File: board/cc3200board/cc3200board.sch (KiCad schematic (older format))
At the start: 26 parts

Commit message: Added datasheet for SPI flash part
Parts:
- removed C?: 10uF, ~, symbol CPSMALL
- removed U?: CC3200R1M2RGCR, VQFN64, symbol CC3200R1M2RGCR
- added C12: 10uF, ~, symbol CPSMALL
- added C46: 10pF, ~, symbol CPSMALL
- added R2, R3, R4: 100K, ~, symbol R
- added U?: CC3200R1M2RGCR, VQFN64, symbol CC3200R1M2RGCR
- added U?: N25Q128A13ESE40E, ~, symbol N25Q128A13ESE40E
- C24: renamed from C?; value 10uF -> 10pF
- X1: renamed from X?; value CRYSTAL -> 32.768kH
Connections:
- wire segments 95 -> 112
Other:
- moved on the sheet: L2, L3, L8, R1, X1

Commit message: Finalized power/RF subsystems for CC3200board
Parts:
- added C42: 6.2pF, ~, symbol CPsmall
- added C49: 10pF, ~, symbol CPsmall
- added C9: 1.0pF, ~, symbol CPsmall
- added E1: ANT, symbol ANT
- added F1: FLT24, symbol FLT24
- added L1: 3.6nH, ~, symbol INDUCTOR_SMALL
- added X2: 40M, symbol 4-PIN_XTAL
- C1, C10, C11, C12, C13, C14, C15, C16, C17, C18, C19, C2, C20, C22, C23, C24, C3, C4, C46, C5, C8: symbol CPSMALL -> CPsmall
- gave numbers to parts that had none: 1
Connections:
- wire segments 112 -> 174

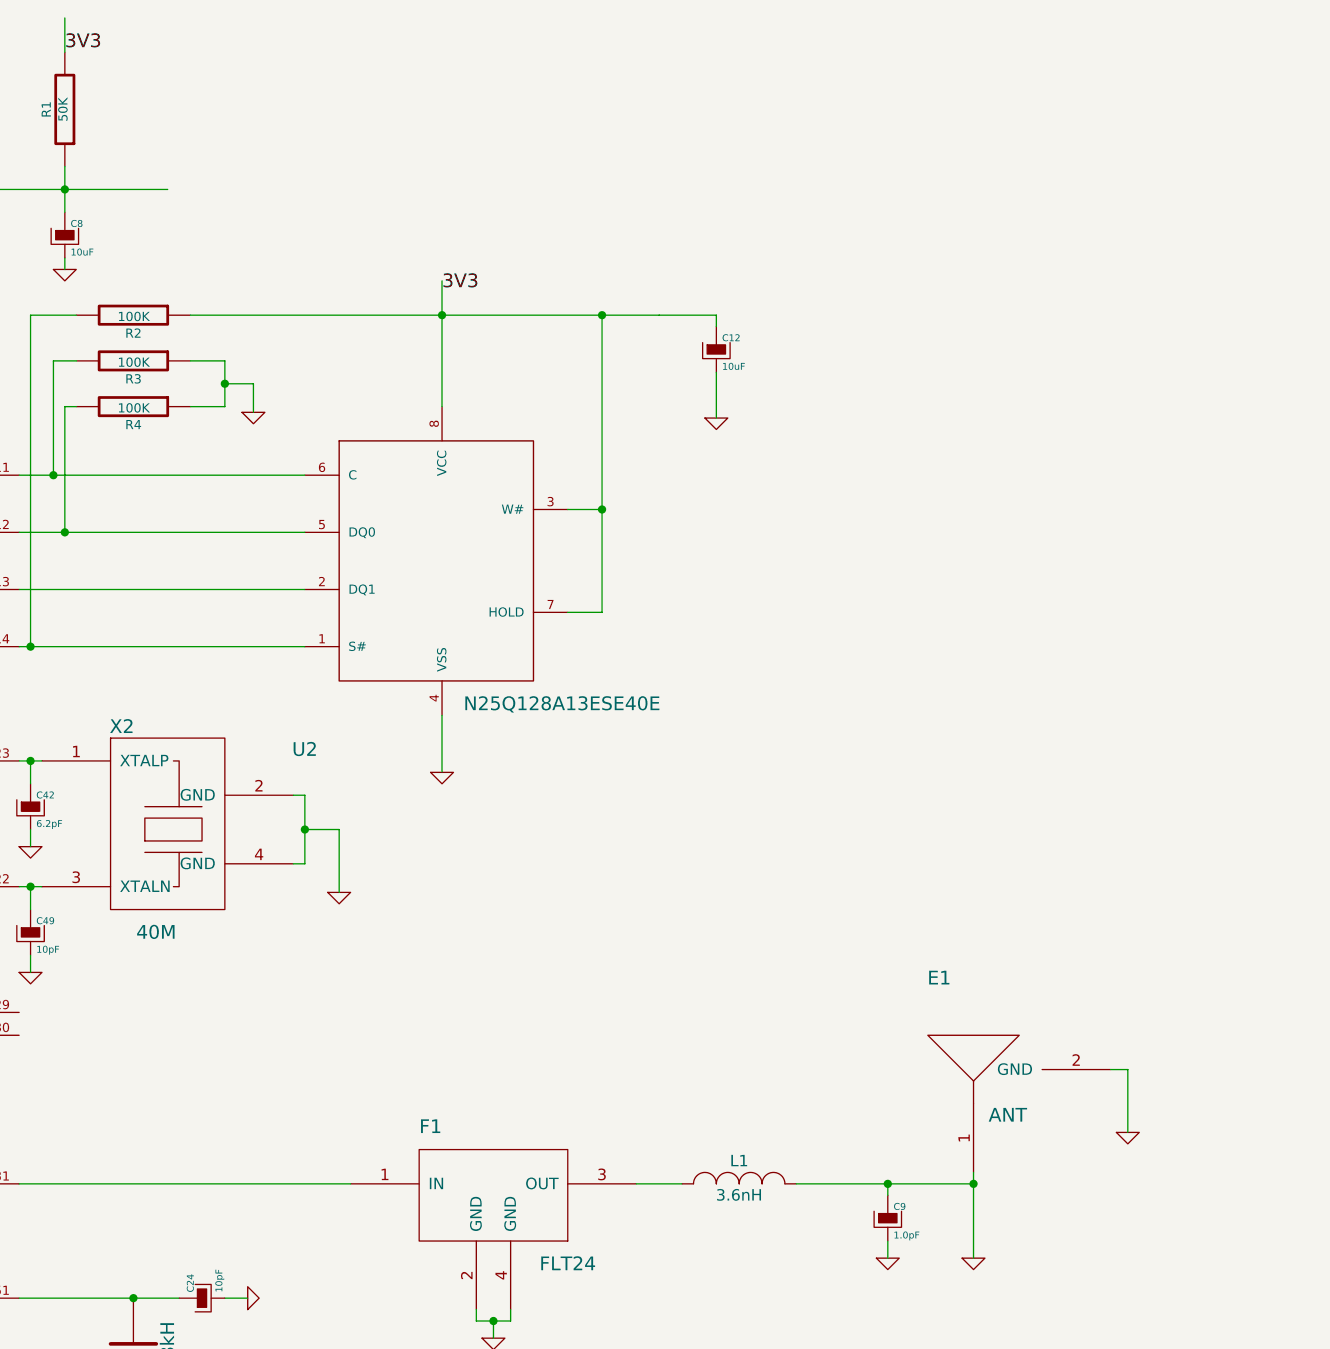
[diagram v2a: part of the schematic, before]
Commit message: Added initial GPIO/JTAG/SOP breakout pins. Impedance controlled traces labelled.
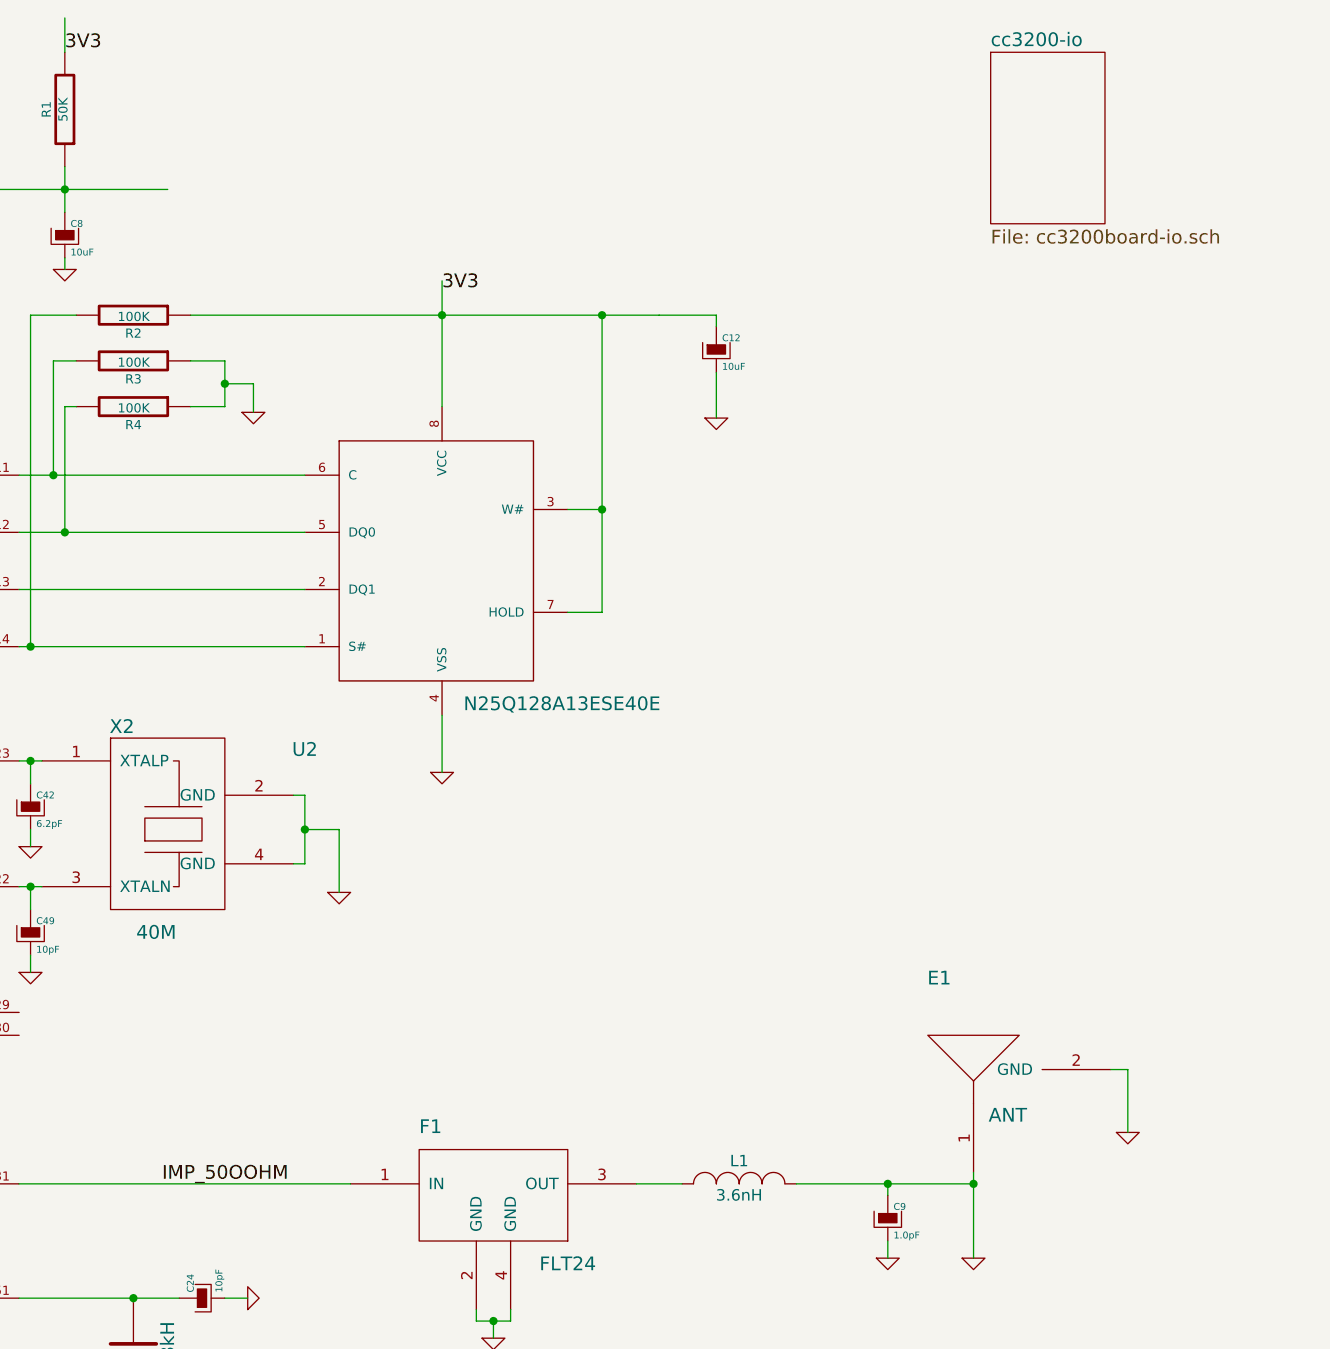
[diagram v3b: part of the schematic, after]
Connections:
- net labels added: IMP_50OOHM
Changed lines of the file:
@@
 $Descr A4 11693 8268
 encoding utf-8
-Sheet 1 1
+Sheet 1 2
 Title ""
 Date "31 oct 2014"
@@
 	8100 2700 8250 2700
 Connection ~ 8250 2700
+$Sheet
+S 9950 700  500  750
+U 5452FF59
+F0 "cc3200-io" 60
+F1 "cc3200board-io.sch" 60
+$EndSheet
+Text Label 6325 5650 0    60   ~ 0
+IMP_50OOHM
 $EndSCHEMATC

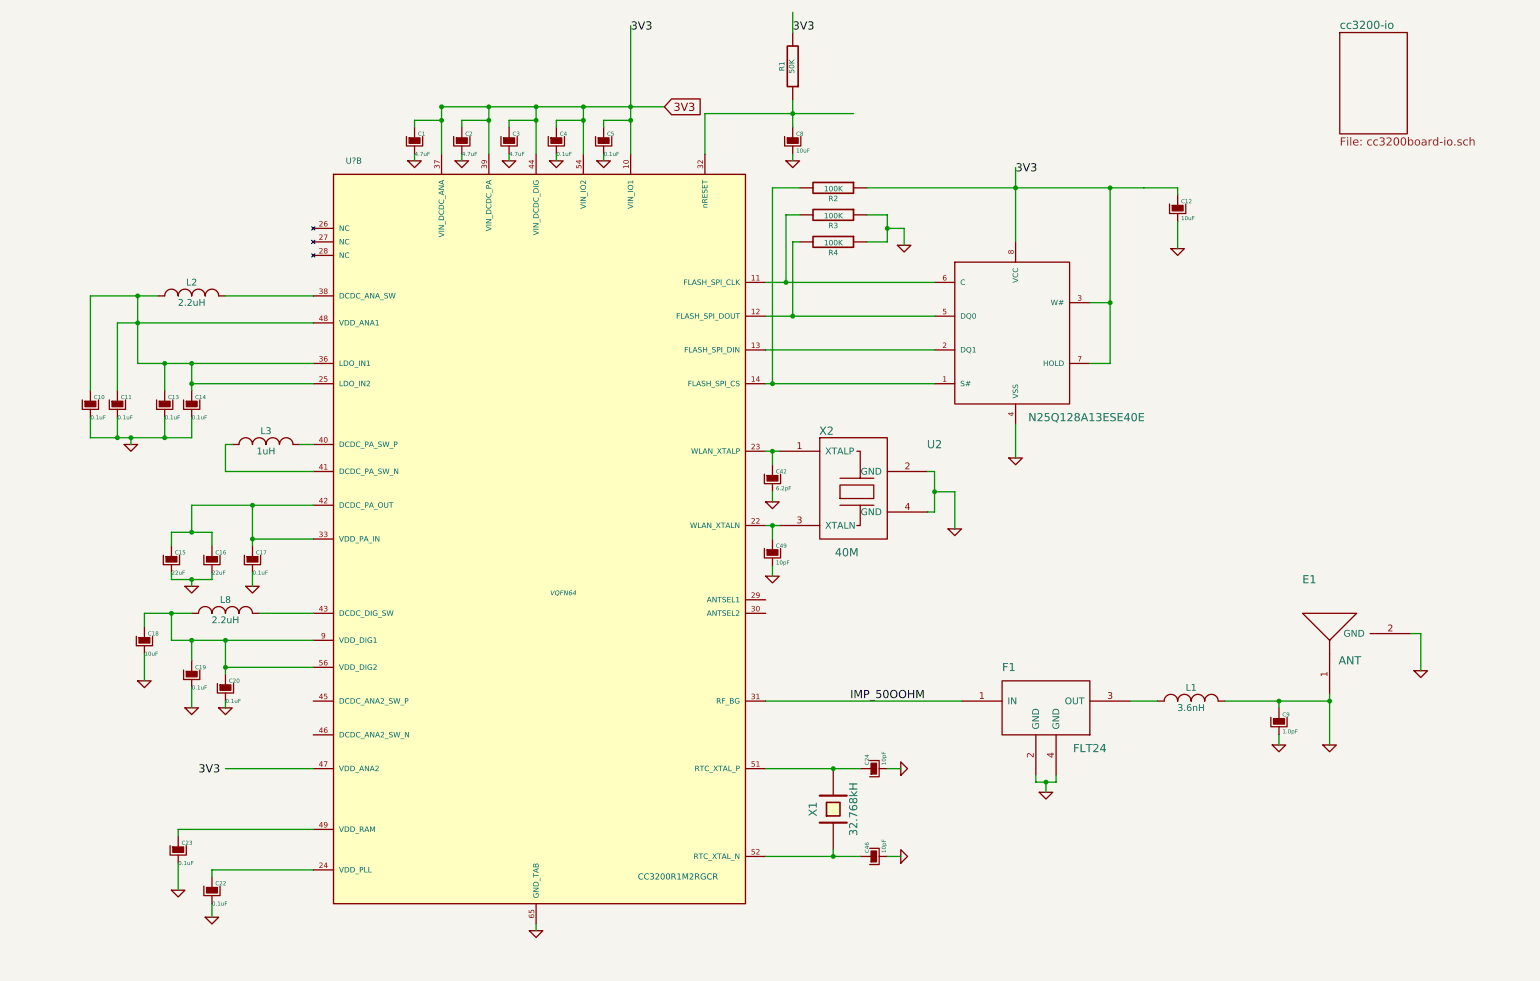
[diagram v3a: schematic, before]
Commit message: Added footprints for all CC3200 components
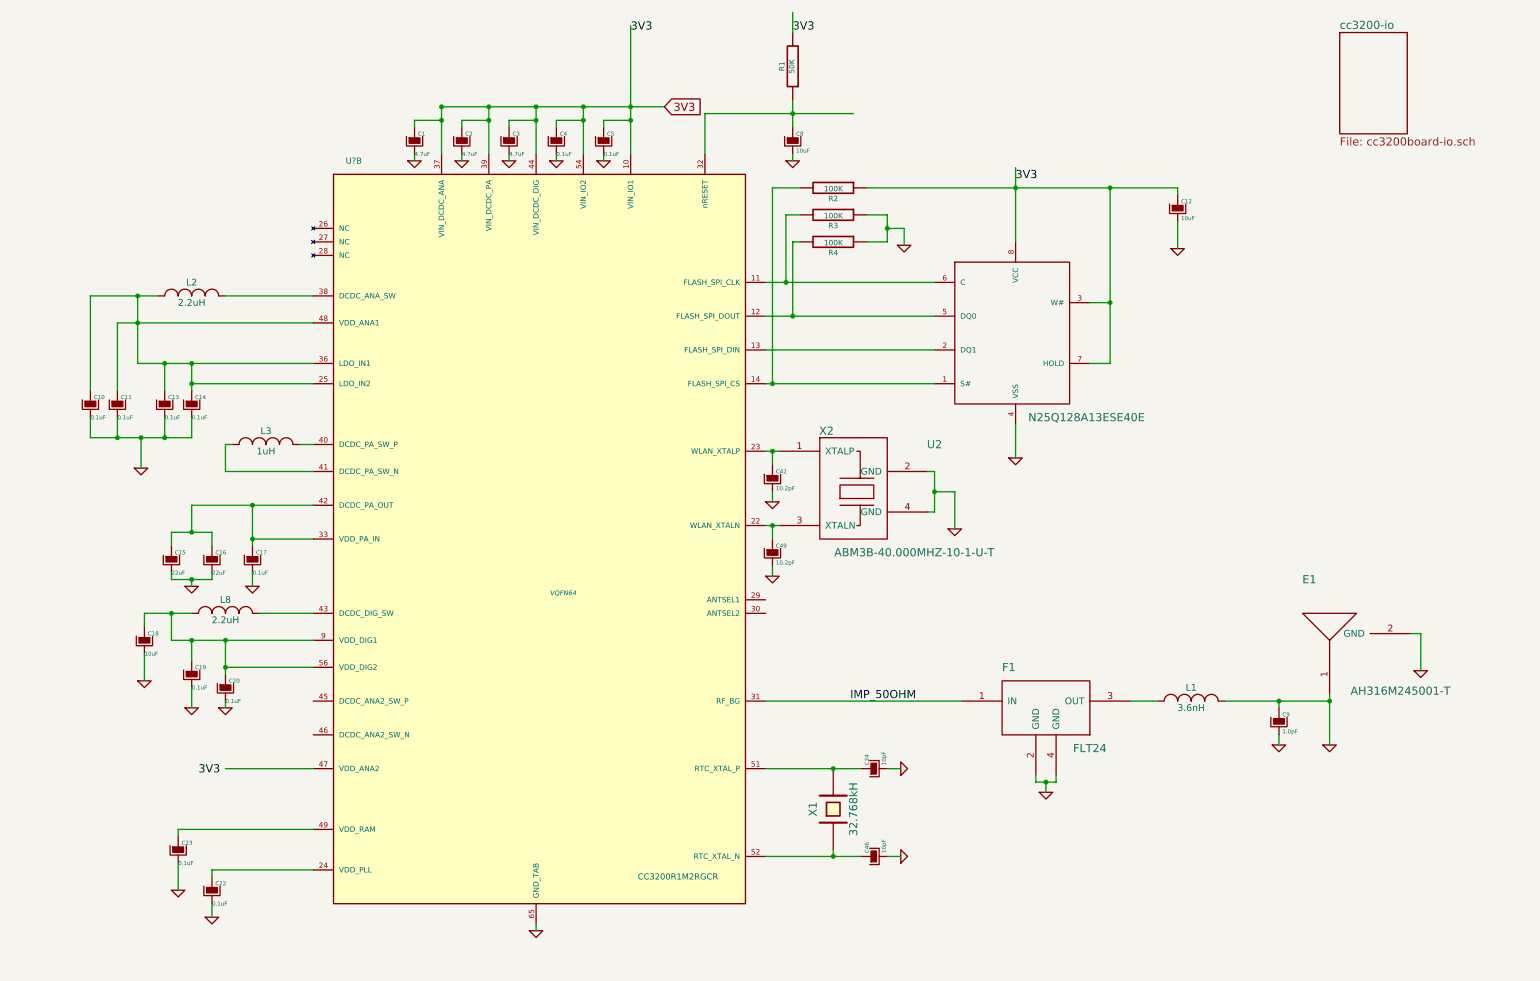
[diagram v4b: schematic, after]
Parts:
- C42: value 6.2pF -> 10.2pF
- C49: value 10pF -> 10.2pF
- E1: value ANT -> AH316M245001-T
- X2: value 40M -> ABM3B-40.000MHZ-10-1-U-T
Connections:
- net labels added: IMP_50OHM
- net labels removed: IMP_50OOHM
- wire segments 174 -> 128
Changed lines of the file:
@@
 L GND #PWR?
 U 1 1 5446219E
-P 1000 3750
-F 0 "#PWR?" H 1000 3750 30  0001 C CNN
-F 1 "GND" H 1000 3680 30  0001 C CNN
-F 2 "" H 1000 3750 60  0000 C CNN
-F 3 "" H 1000 3750 60  0000 C CNN
-	1    1000 3750
+P 1075 3925
+F 0 "#PWR?" H 1075 3925 30  0001 C CNN
+F 1 "GND" H 1075 3855 30  0001 C CNN
+F 2 "" H 1075 3925 60  0000 C CNN
+F 3 "" H 1075 3925 60  0000 C CNN
+	1    1075 3925
 	1    0    0    -1
 $EndComp
@@
 	1    0    0    -1
 $EndComp
-Text Label 7550 1750 0    60   ~ 0
+Text Label 7550 1800 0    60   ~ 0
 3V3
 $Comp
@@
 P 6450 4100
 F 0 "X2" H 6150 4550 60  0000 C CNN
-F 1 "40M" H 6300 3650 60  0000 C CNN
+F 1 "ABM3B-40.000MHZ-10-1-U-T" H 6800 3650 60  0000 C CNN
 F 2 "" H 7250 3550 60  0000 C CNN
 F 3 "" H 7250 3550 60  0000 C CNN
@@
 P 5750 4550
 F 0 "C49" H 5775 4600 30  0000 L CNN
-F 1 "10pF" H 5775 4475 30  0000 L CNN
+F 1 "10.2pF" H 5775 4475 30  0000 L CNN
 F 2 "~" H 5750 4550 60  0000 C CNN
 F 3 "~" H 5750 4550 60  0000 C CNN
@@
 P 5750 4000
 F 0 "C42" H 5775 4050 30  0000 L CNN
-F 1 "6.2pF" H 5775 3925 30  0000 L CNN
+F 1 "10.2pF" H 5775 3925 30  0000 L CNN
 F 2 "~" H 5750 4000 60  0000 C CNN
 F 3 "~" H 5750 4000 60  0000 C CNN
@@
 P 9875 5300
 F 0 "E1" H 9725 5850 60  0000 C CNN
-F 1 "ANT" H 10025 5250 60  0000 C CNN
+F 1 "AH316M245001-T" H 10400 5025 60  0000 C CNN
 F 2 "" H 9875 5300 60  0000 C CNN
 F 3 "" H 9875 5300 60  0000 C CNN
@@
 	700  3350 700  2650
 Wire Wire Line
-	700  2650 1050 2650
-Wire Wire Line
-	1050 2650 1200 2650
+	700  2650 1200 2650
 Connection ~ 1050 2650
 Wire Wire Line
-	1050 3150 1250 3150
-Wire Wire Line
-	1250 3150 1450 3150
-Wire Wire Line
-	1450 3150 2350 3150
+	1050 3150 2350 3150
 Wire Wire Line
 	1450 3300 2350 3300
@@
 Connection ~ 1250 3150
 Wire Wire Line
-	1450 3150 1450 3300
-Wire Wire Line
-	1450 3300 1450 3350
+	1450 3150 1450 3350
 Connection ~ 1450 3300
 Wire Wire Line
@@
 	1600 7250 1600 7150
 Wire Wire Line
-	5900 1200 5900 1300
-Wire Wire Line
-	5900 1300 5900 1400
-Wire Wire Line
-	5250 1300 5900 1300
-Wire Wire Line
-	5900 1300 6350 1300
+	5900 1200 5900 1400
+Wire Wire Line
+	5250 1300 6350 1300
 Connection ~ 5900 1300
 Wire Wire Line
 	5900 1600 5900 1650
 Wire Wire Line
-	5700 6800 6200 6800
-Wire Wire Line
-	6200 6800 6400 6800
+	5700 6800 6400 6800
 Connection ~ 6200 6800
 Wire Wire Line
@@
 	4500 1650 4500 1600
 Wire Wire Line
-	3300 1250 3650 1250
-Wire Wire Line
-	3650 1250 4000 1250
-Wire Wire Line
-	4000 1250 4350 1250
-Wire Wire Line
-	4350 1250 4700 1250
-Wire Wire Line
-	4700 1250 4950 1250
+	3300 1250 4950 1250
 Wire Wire Line
 	4150 1400 4150 1350
@@
 	4150 1350 4350 1350
 Wire Wire Line
-	4350 1250 4350 1350
-Wire Wire Line
-	4350 1350 4350 1600
+	4350 1250 4350 1600
 Connection ~ 4350 1250
 Connection ~ 4350 1350
 Wire Wire Line
-	4000 1250 4000 1350
-Wire Wire Line
-	4000 1350 4000 1600
+	4000 1250 4000 1600
 Connection ~ 4000 1250
 Wire Wire Line
@@
 Connection ~ 4000 1350
 Wire Wire Line
-	3650 1250 3650 1350
-Wire Wire Line
-	3650 1350 3650 1600
+	3650 1250 3650 1600
 Connection ~ 3650 1250
 Wire Wire Line
@@
 Connection ~ 3650 1350
 Wire Wire Line
-	3300 1250 3300 1350
-Wire Wire Line
-	3300 1350 3300 1600
+	3300 1250 3300 1600
 Connection ~ 3300 1250
 Wire Wire Line
@@
 Connection ~ 3300 1350
 Wire Wire Line
-	4700 650  4700 1250
-Wire Wire Line
-	4700 1250 4700 1350
-Wire Wire Line
-	4700 1350 4700 1600
+	4700 650  4700 1600
 Wire Wire Line
 	4500 1400 4500 1350
@@
 	5900 550  5900 700
 Wire Wire Line
-	5700 6150 6200 6150
-Wire Wire Line
-	6200 6150 6400 6150
+	5700 6150 6400 6150
 Connection ~ 6200 6150
 Wire Wire Line
@@
 	1700 2650 2350 2650
 Wire Wire Line
-	900  2850 1050 2850
-Wire Wire Line
-	1050 2850 2350 2850
-Wire Wire Line
-	1050 2650 1050 2850
-Wire Wire Line
-	1050 2850 1050 3150
+	900  2850 2350 2850
+Wire Wire Line
+	1050 2650 1050 3150
 Connection ~ 1050 2850
 Connection ~ 1450 3150
@@
 	1450 3700 1450 3550
 Wire Wire Line
-	700  3700 900  3700
-Wire Wire Line
-	900  3700 1000 3700
-Wire Wire Line
-	1000 3700 1250 3700
-Wire Wire Line
-	1250 3700 1450 3700
-Wire Wire Line
-	1000 3700 1000 3750
+	700  3700 1450 3700
+Wire Wire Line
+	1075 3700 1075 3925
 Wire Wire Line
 	1250 3550 1250 3700
@@
 Wire Wire Line
 	900  3550 900  3700
-Connection ~ 1000 3700
+Connection ~ 1075 3700
 Connection ~ 900  3700
 Wire Wire Line
-	1450 4200 1900 4200
-Wire Wire Line
-	1900 4200 2350 4200
+	1450 4200 2350 4200
 Wire Wire Line
 	2350 4450 1900 4450
 Wire Wire Line
-	1900 4200 1900 4450
-Wire Wire Line
-	1900 4450 1900 4500
+	1900 4200 1900 4500
 Connection ~ 1900 4450
 Wire Wire Line
 	2350 5400 1700 5400
 Wire Wire Line
-	1700 5200 1700 5400
-Wire Wire Line
-	1700 5400 1700 5450
+	1700 5200 1700 5450
 Wire Wire Line
 	1450 5350 1450 5200
 Wire Wire Line
-	1300 5200 1450 5200
-Wire Wire Line
-	1450 5200 1700 5200
-Wire Wire Line
-	1700 5200 2350 5200
+	1300 5200 2350 5200
 Connection ~ 1700 5200
 Connection ~ 1700 5400
 Wire Wire Line
-	1100 5000 1300 5000
-Wire Wire Line
-	1300 5000 1450 5000
+	1100 5000 1450 5000
 Wire Wire Line
 	1100 5000 1100 5100
@@
 	1300 4500 1300 4400
 Wire Wire Line
-	1300 4400 1450 4400
-Wire Wire Line
-	1450 4400 1600 4400
+	1300 4400 1600 4400
 Wire Wire Line
 	1600 4400 1600 4500
@@
 	1300 4700 1300 4750
 Wire Wire Line
-	1300 4750 1450 4750
-Wire Wire Line
-	1450 4750 1600 4750
+	1300 4750 1600 4750
 Wire Wire Line
 	1600 4750 1600 4700
@@
 Connection ~ 1450 4750
 Wire Wire Line
-	5700 2550 5850 2550
-Wire Wire Line
-	5850 2550 6950 2550
+	5700 2550 6950 2550
 Wire Wire Line
 	5700 3050 6950 3050
 Wire Wire Line
-	5700 3300 5750 3300
-Wire Wire Line
-	5750 3300 6950 3300
-Wire Wire Line
-	7550 1700 7550 1850
-Wire Wire Line
-	7550 1850 7550 2250
-Wire Wire Line
-	6450 1850 7550 1850
-Wire Wire Line
-	7550 1850 8250 1850
-Wire Wire Line
-	8250 1850 8500 1850
-Wire Wire Line
-	8500 1850 8750 1850
+	5700 3300 6950 3300
+Wire Wire Line
+	7550 1700 7550 2250
+Wire Wire Line
+	6450 1850 8750 1850
 Connection ~ 7550 1850
 Wire Wire Line
@@
 	6450 2050 6600 2050
 Wire Wire Line
-	5700 2800 5900 2800
-Wire Wire Line
-	5900 2800 6950 2800
+	5700 2800 6950 2800
 Wire Wire Line
 	5950 2250 5900 2250
@@
 	6600 2250 6450 2250
 Wire Wire Line
-	6600 2050 6600 2150
-Wire Wire Line
-	6600 2150 6600 2250
+	6600 2050 6600 2250
 Wire Wire Line
 	6600 2150 6725 2150
@@
 	8750 2100 8750 2300
 Wire Wire Line
-	5700 4350 5750 4350
-Wire Wire Line
-	5750 4350 5800 4350
-Wire Wire Line
-	5700 3800 5750 3800
-Wire Wire Line
-	5750 3800 5800 3800
+	5700 4350 5800 4350
+Wire Wire Line
+	5700 3800 5800 3800
 Wire Wire Line
 	6900 3950 6950 3950
 Wire Wire Line
-	6950 3950 6950 4100
-Wire Wire Line
-	6950 4100 6950 4250
+	6950 3950 6950 4250
 Wire Wire Line
 	6950 4250 6900 4250
@@
 	7700 6200 7700 6250
 Wire Wire Line
-	7700 6250 7775 6250
-Wire Wire Line
-	7775 6250 7850 6250
+	7700 6250 7850 6250
 Wire Wire Line
 	7850 6250 7850 6200
@@
 	8400 5650 8600 5650
 Wire Wire Line
-	9100 5650 9500 5650
-Wire Wire Line
-	9500 5650 9875 5650
-Wire Wire Line
-	9875 5600 9875 5650
-Wire Wire Line
-	9875 5650 9875 5975
+	9100 5650 9875 5650
+Wire Wire Line
+	9875 5600 9875 5975
 Connection ~ 9875 5650
 Wire Wire Line
@@
 	6725 2150 6725 2275
 Wire Wire Line
-	8100 3150 8250 3150
-Wire Wire Line
-	8250 3150 8250 2700
-Wire Wire Line
-	8250 2700 8250 1850
+	8250 3150 8100 3150
+Wire Wire Line
+	8250 1850 8250 3150
 Connection ~ 8250 1850
 Wire Wire Line
@@
 $EndSheet
 Text Label 6325 5650 0    60   ~ 0
-IMP_50OOHM
+IMP_50OHM
 $EndSCHEMATC
